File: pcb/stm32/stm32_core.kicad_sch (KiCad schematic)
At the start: 1 part

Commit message: Fixed schema
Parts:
- removed U?: STM32G070KBT6, LQFP-32, symbol 2023-02-12_17-09-08:STM32G070KBT6
- added U?: STM32G070KBT6, LQFP-32, symbol 2023-02-13_13-40-03:STM32G070KBT6
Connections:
- net +3.3V: now also U?.4 (VDD)
- net GND: now also U?.5 (VSS)
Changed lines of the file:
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@@
 (kicad_sch (version 20211123) (generator eeschema)
   (paper "A4")
-  (wire (pts (xy 190.5 90.17) (xy 190.5 88.9))
+  (wire (pts (xy 210.82 92.71) (xy 210.82 91.44))
     (stroke (width 0) (type default) (color 0 0 0 0))
   )
-  (wire (pts (xy 110.49 143.51) (xy 110.49 140.97))
+  (wire (pts (xy 100.33 143.51) (xy 100.33 140.97))
     (stroke (width 0) (type default) (color 0 0 0 0))
   )
-  (wire (pts (xy 110.49 140.97) (xy 113.03 140.97))
+  (wire (pts (xy 100.33 140.97) (xy 102.87 140.97))
     (stroke (width 0) (type default) (color 0 0 0 0))
   )
-  (wire (pts (xy 179.07 90.17) (xy 190.5 90.17))
+  (wire (pts (xy 199.39 92.71) (xy 210.82 92.71))
     (stroke (width 0) (type default) (color 0 0 0 0))
   )
-  (symbol (lib_id "power:GND") (at 110.49 143.51 0) (unit 1)
+  (symbol (lib_id "2023-02-13_13-40-03:STM32G070KBT6") (at 102.87 49.53 0) (unit 1)
     (in_bom yes) (on_board yes) (fields_autoplaced)
-    (property "Reference" "#PWR?" (id 0) (at 110.49 149.86 0)
-      (effects (font (size 1.27 1.27)) hide)
-    )
-    (property "Value" "GND" (id 1) (at 110.49 148.59 0))
-    (property "Footprint" "" (id 2) (at 110.49 143.51 0)
-      (effects (font (size 1.27 1.27)) hide)
-    )
-    (property "Datasheet" "" (id 3) (at 110.49 143.51 0)
-      (effects (font (size 1.27 1.27)) hide)
-    )
-    (pin "1")
-  )
-  (symbol (lib_id "2023-02-12_17-09-08:STM32G070KBT6") (at 113.03 46.99 0) (unit 1)
-    (in_bom yes) (on_board yes) (fields_autoplaced)
-    (property "Reference" "U?" (id 0) (at 146.05 35.56 0)
+    (property "Reference" "U?" (id 0) (at 151.13 38.1 0)
       (effects (font (size 1.524 1.524)))
     )
-    (property "Value" "STM32G070KBT6" (id 1) (at 146.05 39.37 0)
+    (property "Value" "STM32G070KBT6" (id 1) (at 151.13 41.91 0)
       (effects (font (size 1.524 1.524)))
     )
-    (property "Footprint" "LQFP-32" (id 2) (at 113.03 46.99 0)
+    (property "Footprint" "LQFP-32" (id 2) (at 102.87 49.53 0)
       (effects (font (size 1.27 1.27) italic) hide)
     )
-    (property "Datasheet" "STM32G070KBT6" (id 3) (at 113.03 46.99 0)
+    (property "Datasheet" "STM32G070KBT6" (id 3) (at 102.87 49.53 0)
       (effects (font (size 1.27 1.27) italic) hide)
     )
@@
     (pin "9")
   )
-  (symbol (lib_id "power:+3.3V") (at 190.5 88.9 0) (unit 1)
+  (symbol (lib_id "power:GND") (at 100.33 143.51 0) (unit 1)
     (in_bom yes) (on_board yes) (fields_autoplaced)
-    (property "Reference" "#PWR?" (id 0) (at 190.5 92.71 0)
+    (property "Reference" "#PWR?" (id 0) (at 100.33 149.86 0)
       (effects (font (size 1.27 1.27)) hide)
     )
-    (property "Value" "+3.3V" (id 1) (at 190.5 83.82 0))
-    (property "Footprint" "" (id 2) (at 190.5 88.9 0)
+    (property "Value" "GND" (id 1) (at 100.33 148.59 0))
+    (property "Footprint" "" (id 2) (at 100.33 143.51 0)
       (effects (font (size 1.27 1.27)) hide)
     )
-    (property "Datasheet" "" (id 3) (at 190.5 88.9 0)
+    (property "Datasheet" "" (id 3) (at 100.33 143.51 0)
       (effects (font (size 1.27 1.27)) hide)
     )
+    (pin "1")
+  )
+  (symbol (lib_id "power:+3.3V") (at 210.82 91.44 0) (unit 1)
+    (in_bom yes) (on_board yes) (fields_autoplaced)
+    (property "Reference" "#PWR?" (id 0) (at 210.82 95.25 0)
+      (effects (font (size 1.27 1.27)) hide)
+    )
+    (property "Value" "+3.3V" (id 1) (at 210.82 86.36 0))
+    (property "Footprint" "" (id 2) (at 210.82 91.44 0)
+      (effects (font (size 1.27 1.27)) hide)
+    )
+    (property "Datasheet" "" (id 3) (at 210.82 91.44 0)
+      (effects (font (size 1.27 1.27)) hide)
+    )

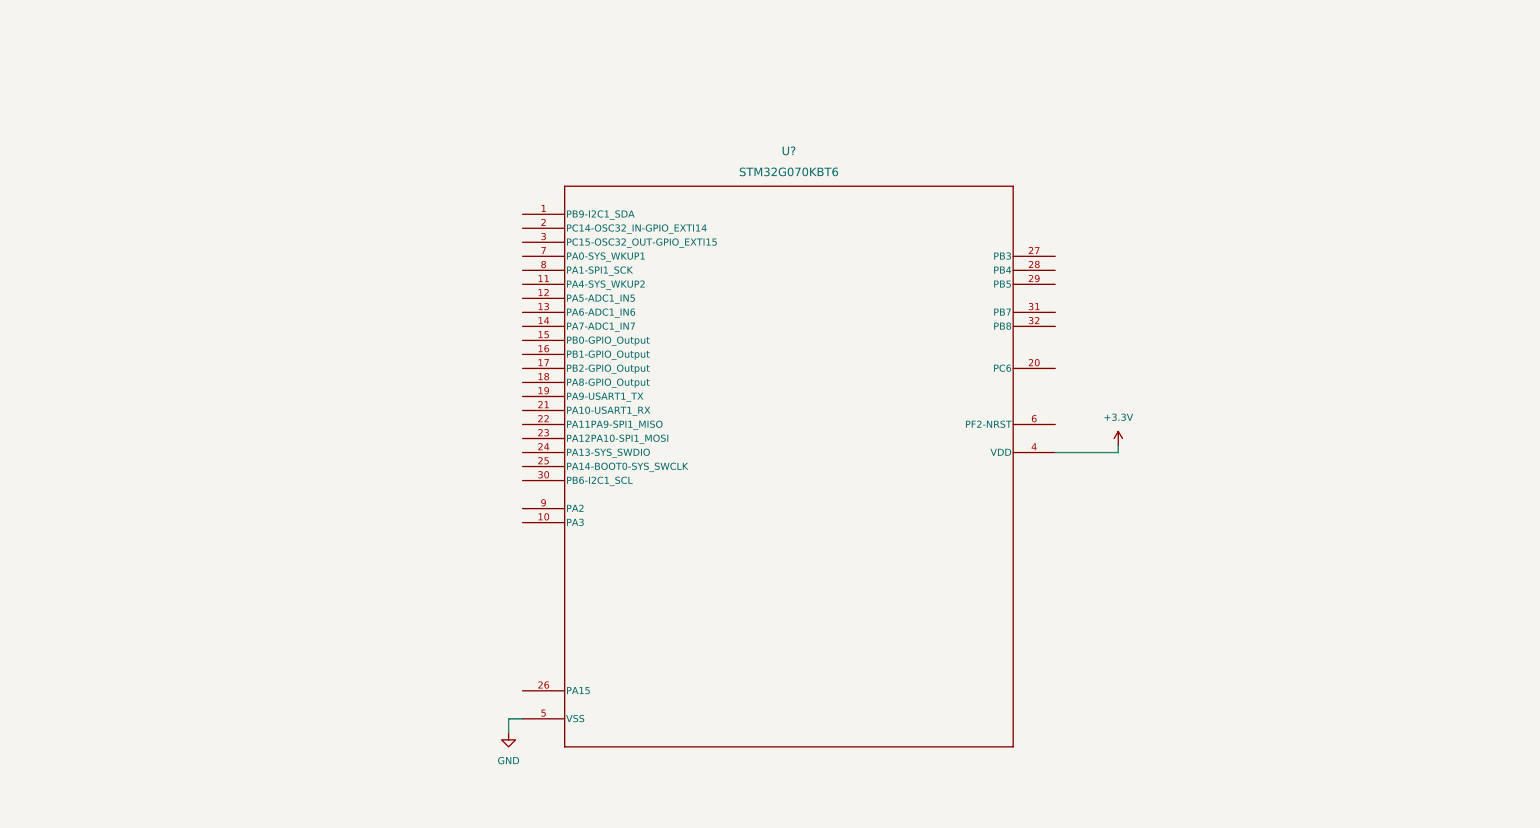
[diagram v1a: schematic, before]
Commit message: Upgrade to kicad7
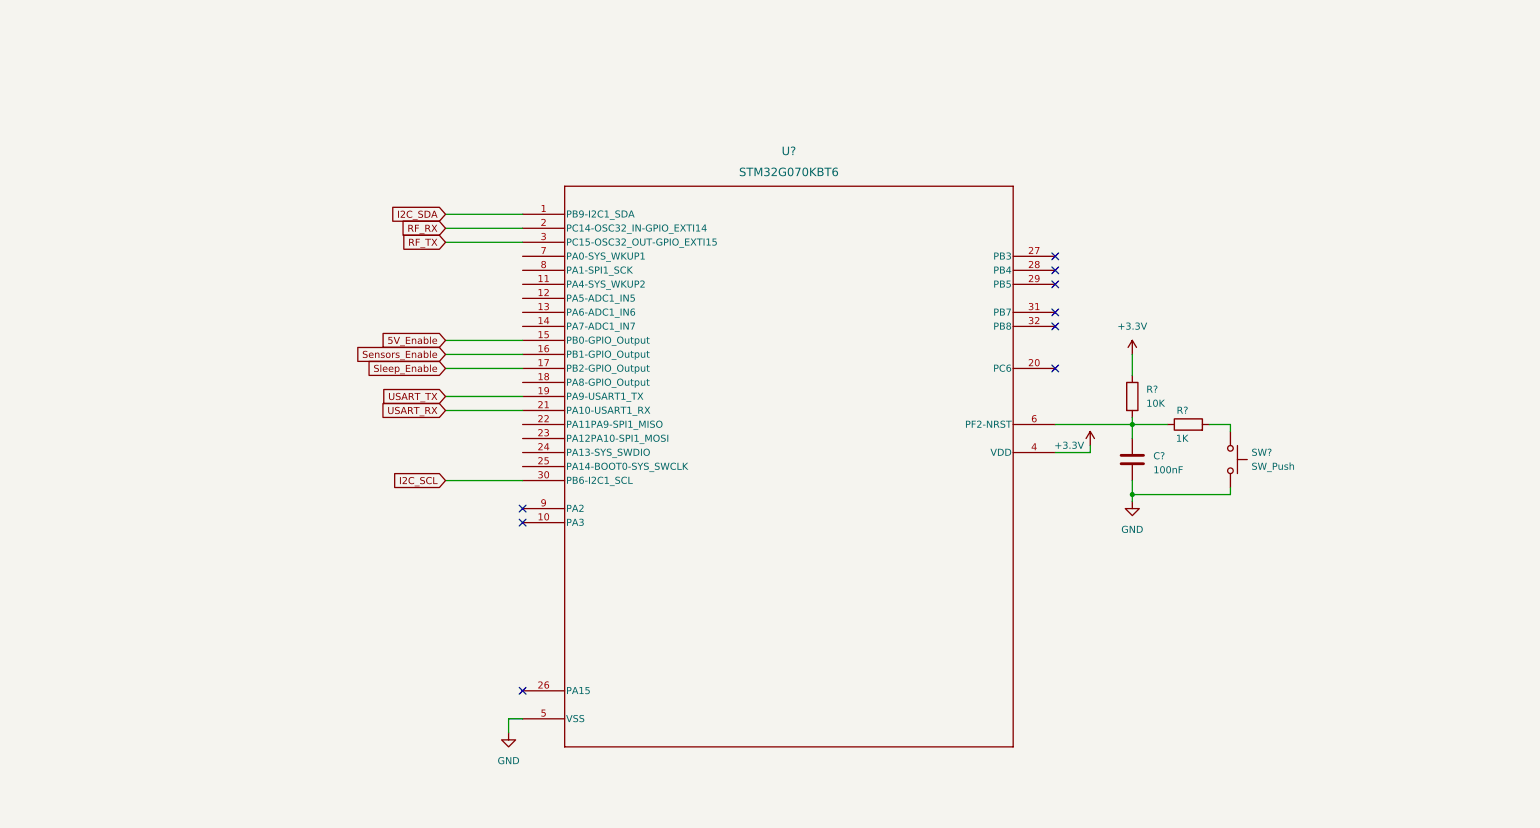
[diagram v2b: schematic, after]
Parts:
- added C?: 100nF, symbol Device:C
- added R?: 1K, symbol Device:R
- added R?: 10K, symbol Device:R
- added SW?: SW_Push, symbol Switch:SW_Push
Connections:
- net +3.3V: now also R?.1
- net GND: now also C?.2, SW?.2
- net I2C_SDA: now reaches U?.1 (PB9-I2C1_SDA)
- net 5V_Enable: now reaches U?.15 (PB0-GPIO_Output)
- net Sensors_Enable: now reaches U?.16 (PB1-GPIO_Output)
- net Sleep_Enable: now reaches U?.17 (PB2-GPIO_Output)
- net USART_TX: now reaches U?.19 (PA9-USART1_TX)
- net RF_RX: now reaches U?.2 (PC14-OSC32_IN-GPIO_EXTI14)
- net USART_RX: now reaches U?.21 (PA10-USART1_RX)
- net RF_TX: now reaches U?.3 (PC15-OSC32_OUT-GPIO_EXTI15)
- net I2C_SCL: now reaches U?.30 (PB6-I2C1_SCL)
- net at U?.6 (PF2-NRST): now also C?.1, R?.1, R?.2
- new net: R?.2, SW?.1
- no-connect marks 0 -> 9

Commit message: Prepared labels for MCU
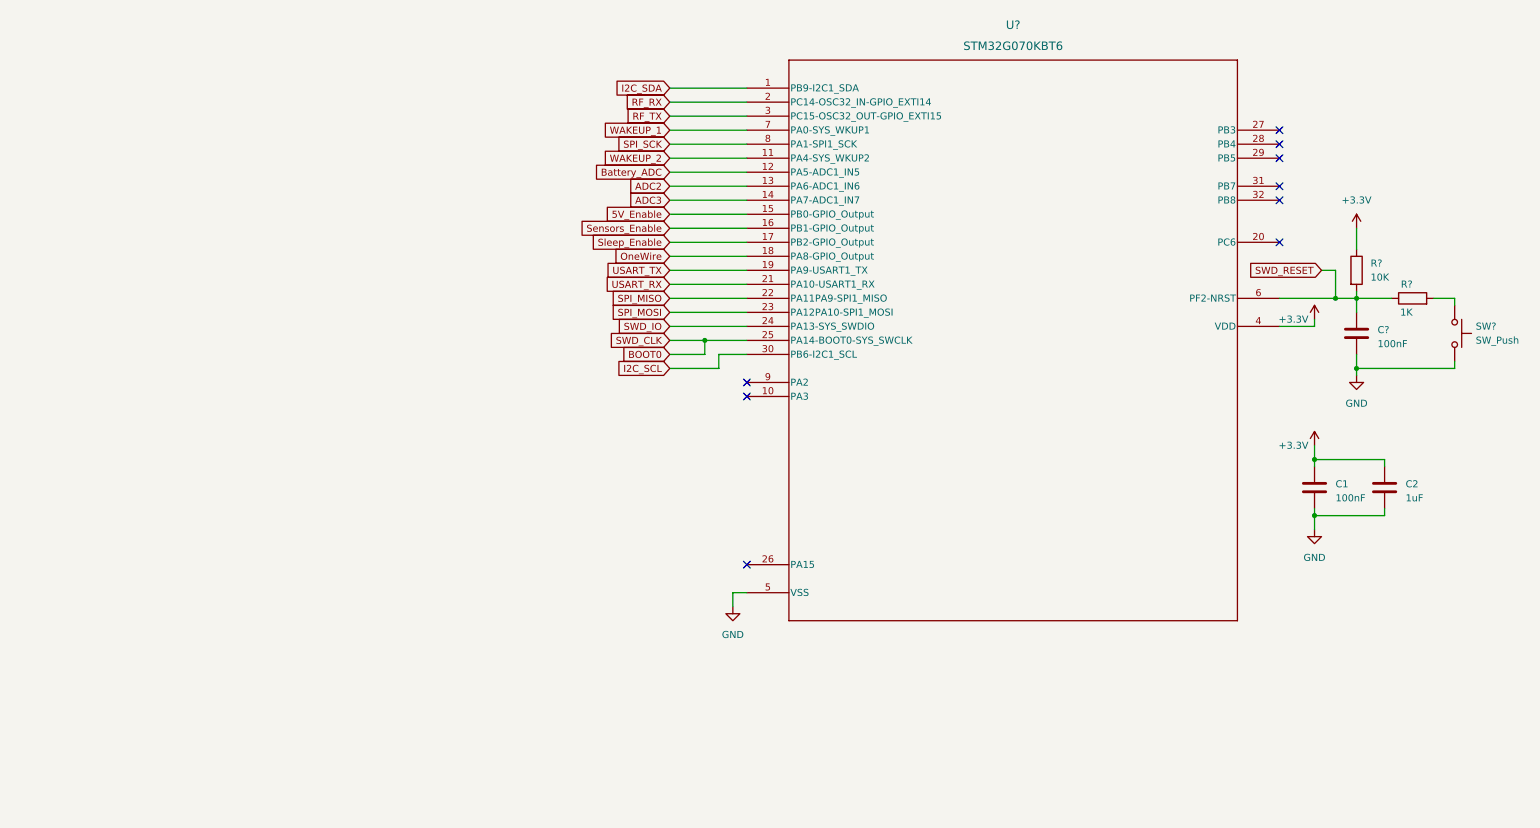
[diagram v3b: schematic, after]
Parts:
- added C1: 100nF, symbol Device:C
- added C2: 1uF, symbol Device:C
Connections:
- net +3.3V: now also C1.1, C2.1
- net GND: now also C1.2, C2.2
- net WAKEUP_2: now reaches U?.11 (PA4-SYS_WKUP2)
- net Battery_ADC: now reaches U?.12 (PA5-ADC1_IN5)
- net ADC2: now reaches U?.13 (PA6-ADC1_IN6)
- net ADC3: now reaches U?.14 (PA7-ADC1_IN7)
- net OneWire: now reaches U?.18 (PA8-GPIO_Output)
- net SPI_MISO: now reaches U?.22 (PA11PA9-SPI1_MISO)
- net SPI_MOSI: now reaches U?.23 (PA12PA10-SPI1_MOSI)
- net SWD_IO: now reaches U?.24 (PA13-SYS_SWDIO)
- net BOOT0: now reaches U?.25 (PA14-BOOT0-SYS_SWCLK)
- net SWD_RESET: now reaches C?.1, R?.1, R?.2, U?.6 (PF2-NRST)
- net WAKEUP_1: now reaches U?.7 (PA0-SYS_WKUP1)
- net SPI_SCK: now reaches U?.8 (PA1-SPI1_SCK)
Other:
- moved on the sheet: C?, R?, SW?, U?

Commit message: Slow progress
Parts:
- added J1: Conn_01x04_Pin, symbol Connector:Conn_01x04_Pin
- added R1, R2: 10K, symbol Device:R
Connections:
- net +3.3V: now also J1.1 (Pin_1), R1.1, R2.1
- net GND: now also J1.4 (Pin_4)
- net I2C_SCL: now also J1.3 (Pin_3), R2.2
- net I2C_SDA: now also J1.2 (Pin_2), R1.2

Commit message: Updated PCB
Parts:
- added J2: Conn_01x06_Pin, symbol Connector:Conn_01x06_Pin
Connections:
- net +3.3V: now also J2.1 (Pin_1)
- net BOOT0: now also J2.2 (Pin_2)
- net GND: now also J2.3 (Pin_3)
- net SWD_IO: now also J2.4 (Pin_4)
- net SWD_RESET: now also J2.5 (Pin_5)
- no-connect marks 9 -> 10
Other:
- note added: "I2C"
- note added: "SWD 6pin"
- moved on the sheet: J1, R1, R2

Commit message: Update pcb
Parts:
- added J3, J5: Conn_02x05_Top_Bottom, symbol Connector_Generic:Conn_02x05_Top_Bottom
- added J4: Conn_01x02_Pin, symbol Connector:Conn_01x02_Pin
- added J6: Conn_01x02_Pin, symbol Connector:Conn_01x03_Pin
- added R3, R4, R5: 10K, symbol Device:R
- added SW1: SW_Push, symbol Switch:SW_Push
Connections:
- net +3.3V: now also J4.1 (Pin_1), J6.1 (Pin_1), R5.2, SW1.1
- net 5V_Enable: now also J5.4 (Pin_4)
- net BOOT0: now also J3.8 (Pin_8)
- net GND: now also J3.2 (Pin_2), J3.7 (Pin_7), J5.10 (Pin_10), J5.5 (Pin_5), J6.3 (Pin_3), R3.2, R4.2
- net I2C_SCL: now also J5.8 (Pin_8)
- net I2C_SDA: now also J5.3 (Pin_3)
- net OneWire: now also J5.7 (Pin_7), R5.1
- net RF_RX: now also J5.1 (Pin_1)
- net RF_TX: now also J5.6 (Pin_6)
- net SWD_IO: now also J3.6 (Pin_6)
- net SWD_RESET: now also J3.1 (Pin_1)
- net Sensors_Enable: now also J5.9 (Pin_9)
- net Sleep_Enable: now also J5.2 (Pin_2)
- net WAKEUP_1: now also R4.1
- net WAKEUP_2: now also J6.2 (Pin_2), R3.1, SW1.2
- new net: J3.4 (Pin_4), J3.9 (Pin_9), J4.2 (Pin_2)
- no-connect marks 10 -> 13
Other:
- note added: "DEBUG"
- note added: "OneWire Pullup"
- note added: "ST-Link v2 clone"
- note added: "USR Wakeup"
- note added: "Wakeup"

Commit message: Added all hiearchical labels
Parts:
- added R6: 10K, symbol Device:R
- added SW2: SW_Push, symbol Switch:SW_Push
- gave numbers to parts that had none: 5
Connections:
- net +3.3V: now also SW2.1
- net BOOT0: now also R6.1, SW2.2
- net GND: now also R6.2
- net ADC2 renamed SPI_SS1
- net ADC3 renamed SPI_SS2
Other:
- note added: "Boot0"
